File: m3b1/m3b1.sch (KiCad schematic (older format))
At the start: 16 parts, among them P5 MicroD-37Pins, Q1 MD3251, Q2 MD3251, U1 MC307, U2 MC306, U3 MC306, U4 MC306, U5 MC302, U6 MC306, U7 MC306, U8 MC301, U9 MC301

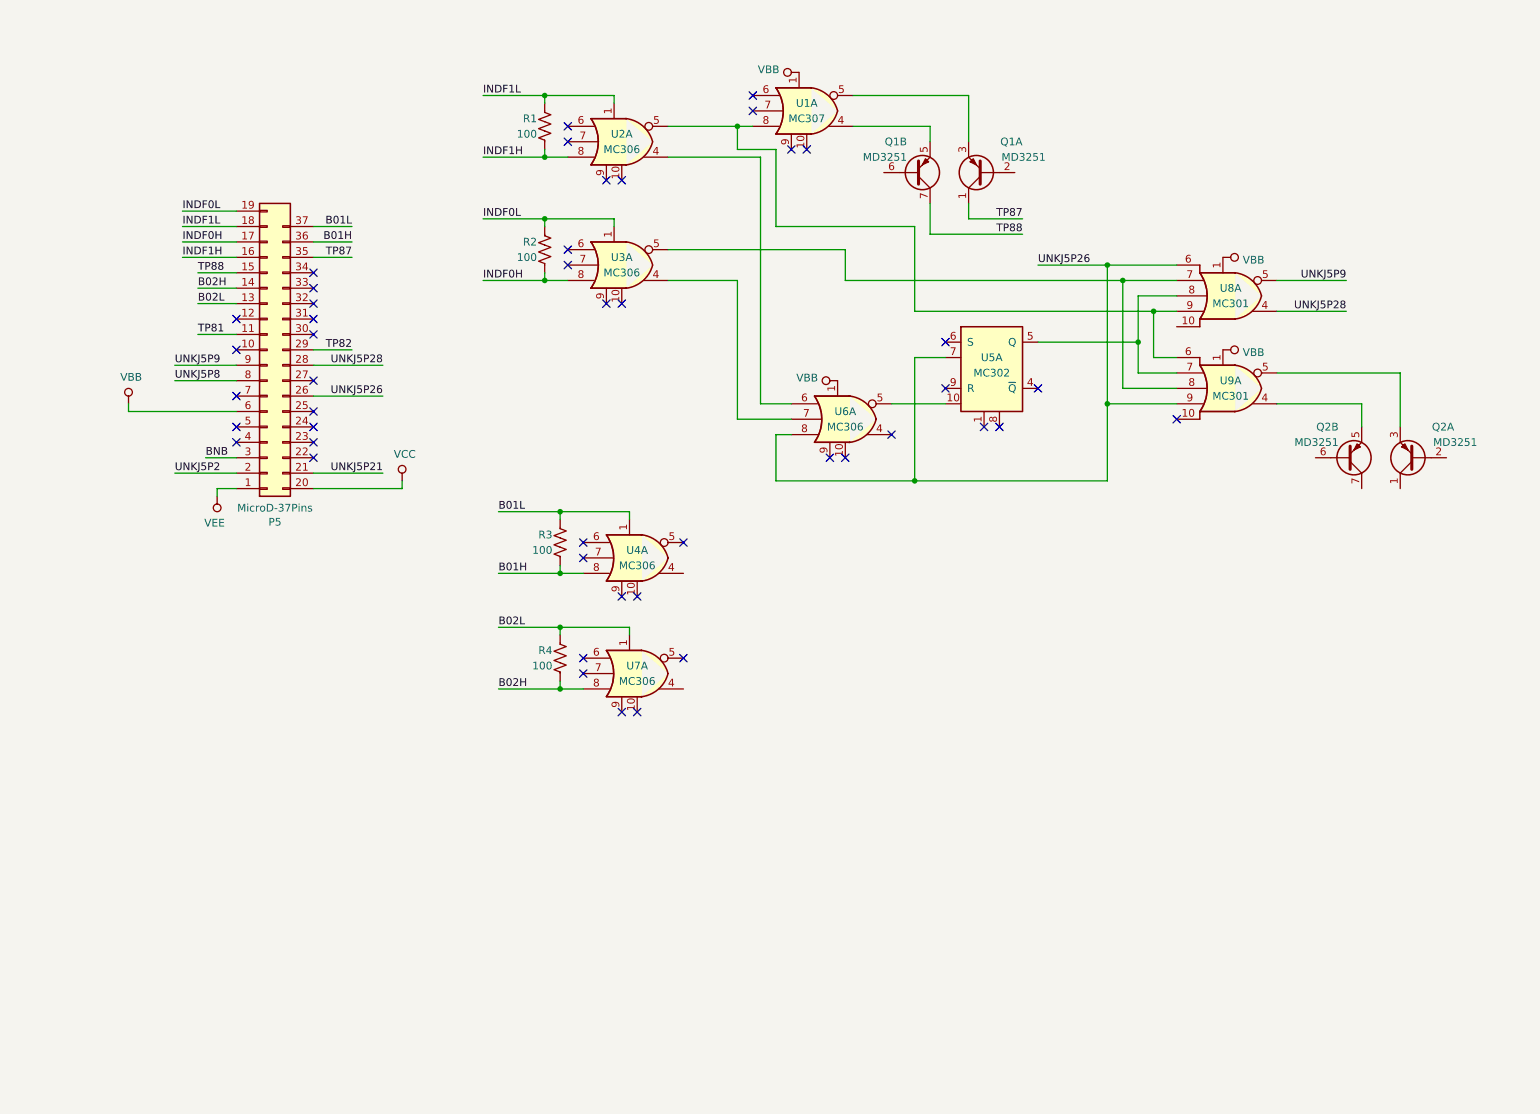
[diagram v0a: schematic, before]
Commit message: Completed initial schematic for module 3 board 1.
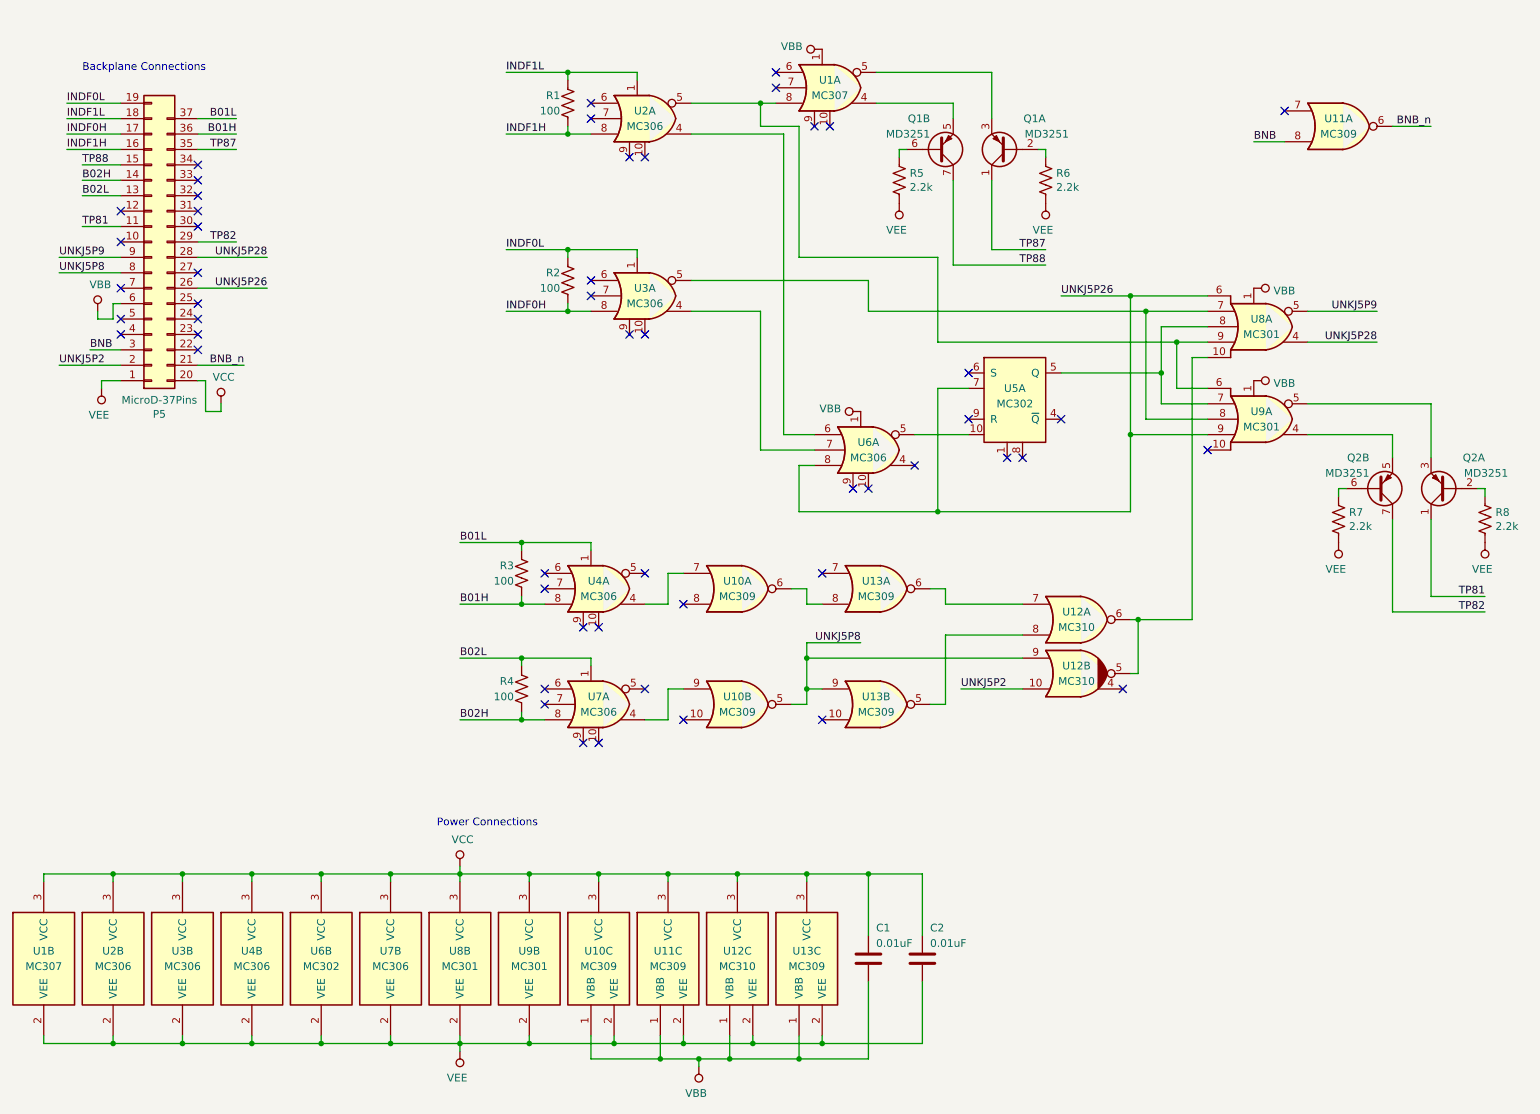
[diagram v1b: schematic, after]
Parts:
- added C1, C2: 0.01uF, symbol Device:C
- added R5, R6, R7, R8: 2.2k, symbol Device:R_US
- added unit 2 of U1
- added U10, U11, U13: MC309, symbol gn_buffer:MC309
- added U12: MC310, symbol gn_buffer:MC310
- added unit 2 of U2
- added unit 2 of U3
- added unit 2 of U4
- added unit 2 of U6
- added unit 2 of U7
- added unit 2 of U8
- added unit 2 of U9
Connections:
- net BNB: now also U11.8
- net TP81: now also Q2.1 (C1)
- net TP82: now also Q2.7 (C2)
- net UNKJ5P2: now also U12.10
- net UNKJ5P8: now also U10.5, U12.9, U13.9
- net VBB: now also C1.2, U10.1 (VBB), U11.1 (VBB), U12.1 (VBB), U13.1 (VBB)
- net VCC: now also C1.1, C2.1, U1.3 (VCC), U10.3 (VCC), U11.3 (VCC), U12.3 (VCC), U13.3 (VCC), U2.3 (VCC), U3.3 (VCC), U4.3 (VCC), U6.3 (VCC), U7.3 (VCC), U8.3 (VCC), U9.3 (VCC)
- net VEE: now also C2.2, R5.2, R6.2, R7.2, R8.2, U1.2 (VEE), U10.2 (VEE), U11.2 (VEE), U12.2 (VEE), U13.2 (VEE), U2.2 (VEE), U3.2 (VEE), U4.2 (VEE), U6.2 (VEE), U7.2 (VEE), U8.2 (VEE), U9.2 (VEE)
- net at U4.4: now also U10.7
- net at Q1.2 (B1): now also R6.1
- net at Q1.6 (B2): now also R5.1
- net at U7.4: now also U10.9
- net at U8.10: now also U12.5, U12.6
- net at Q2.2 (B1): now also R8.1
- net at Q2.6 (B2): now also R7.1
- net UNKJ5P21 renamed BNB_n
- net BNB_n: now also U11.6
- new net: U10.6, U13.8
- new net: U12.7, U13.6
- new net: U12.8, U13.5
- no-connect marks 46 -> 52
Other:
- note added: "Backplane Connections"
- note added: "Power Connections"
- moved on the sheet: P5, Q1A, Q1B, Q2A, Q2B, R1, R2, R3, R4, U1A, U2A, U3A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

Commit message: Eradicated net names taken from ME901-0666 -- the pinout was completely changed from early revs of that document.
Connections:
- net B01H renamed IN01H
- net B01L renamed IN01L
- net B02H renamed IN02H
- net B02L renamed IN02L
- net BNB renamed MC41
- net BNB_n renamed MC41_n
- net INDF0H renamed MC79
- net INDF0L renamed MC80
- net INDF1H renamed MC77
- net INDF1L renamed MC78
- net TP81 renamed MC81
- net TP82 renamed MC82
- net TP87 renamed MC87
- net TP88 renamed MC88
- net UNKJ5P26 renamed MC01
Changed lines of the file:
@@
 $EndDescr
 Text Label 2050 1500 2    50   ~ 0
-TP87
+MC87
 Wire Wire Line
 	1800 1500 2050 1500
 Text Label 2050 2100 2    50   ~ 0
-TP82
+MC82
 Wire Wire Line
 	1800 2100 2050 2100
 Text Label 1050 2000 0    50   ~ 0
-TP81
+MC81
 Wire Wire Line
 	1300 2000 1050 2000
-Text Label 950  1200 0    50   ~ 0
-INDF0L
-Wire Wire Line
-	1300 1200 950  1200
-Text Label 950  1400 0    50   ~ 0
-INDF0H
-Wire Wire Line
-	1300 1400 950  1400
-Text Label 950  1300 0    50   ~ 0
-INDF1L
-Wire Wire Line
-	1300 1300 950  1300
-Text Label 950  1500 0    50   ~ 0
-INDF1H
-Wire Wire Line
-	1300 1500 950  1500
+Text Label 1050 1200 0    50   ~ 0
+MC80
+Wire Wire Line
+	1300 1200 1050 1200
+Text Label 1050 1400 0    50   ~ 0
+MC79
+Wire Wire Line
+	1300 1400 1050 1400
+Text Label 1050 1300 0    50   ~ 0
+MC78
+Wire Wire Line
+	1300 1300 1050 1300
+Text Label 1050 1500 0    50   ~ 0
+MC77
+Wire Wire Line
+	1300 1500 1050 1500
 Text Label 1100 2800 0    50   ~ 0
-BNB
+MC41
 Wire Wire Line
 	1300 2800 1100 2800
 Text Label 1050 1800 0    50   ~ 0
-B02L
+IN02L
 Wire Wire Line
 	1300 1800 1050 1800
 Text Label 1050 1700 0    50   ~ 0
-B02H
+IN02H
 Wire Wire Line
 	1300 1700 1050 1700
 Text Label 2050 1300 2    50   ~ 0
-B01L
+IN01L
 Wire Wire Line
 	1800 1300 2050 1300
 Text Label 2050 1400 2    50   ~ 0
-B01H
+IN01H
 Wire Wire Line
 	1800 1400 2050 1400
@@
 	1300 1600 1050 1600
 Text Label 1050 1600 0    50   ~ 0
-TP88
+MC88
 NoConn ~ 1800 1700
 Wire Wire Line
@@
 Connection ~ 3900 4450
 Text Label 3500 4450 0    50   ~ 0
-B01H
+IN01H
 Wire Wire Line
 	3900 4050 3500 4050
 Connection ~ 3900 4050
 Text Label 3500 4050 0    50   ~ 0
-B01L
+IN01L
 NoConn ~ 4700 4250
 $Comp
@@
 Connection ~ 4200 2550
 Text Label 3800 2550 0    50   ~ 0
-INDF0H
+MC79
 Wire Wire Line
 	4200 2150 3800 2150
 Connection ~ 4200 2150
 Text Label 3800 2150 0    50   ~ 0
-INDF0L
+MC80
 $Comp
 L gn_buffer:MC306 U2
@@
 Connection ~ 4200 1400
 Text Label 3800 1400 0    50   ~ 0
-INDF1H
+MC77
 Wire Wire Line
 	4200 1000 3800 1000
 Connection ~ 4200 1000
 Text Label 3800 1000 0    50   ~ 0
-INDF1L
+MC78
 $Comp
 L gn_buffer:MC307 U1
@@
 	6950 2150 7300 2150
 Text Label 7300 2150 2    50   ~ 0
-TP87
+MC87
 Text Label 7300 2250 2    50   ~ 0
-TP88
+MC88
 $Comp
 L gn_buffer:MC306 U7
@@
 Connection ~ 3900 5200
 Text Label 3500 5200 0    50   ~ 0
-B02H
+IN02H
 Wire Wire Line
 	3900 4800 3500 4800
 Connection ~ 3900 4800
 Text Label 3500 4800 0    50   ~ 0
-B02L
+IN02L
 NoConn ~ 4700 5000
 $Comp
@@
 UNKJ5P28
 Wire Wire Line
-	1800 2400 2250 2400
-Text Label 2250 2400 2    50   ~ 0
-UNKJ5P26
+	1800 2400 2050 2400
+Text Label 2050 2400 2    50   ~ 0
+MC01
 Wire Wire Line
 	1800 2900 2100 2900
 Text Label 2100 2900 2    50   ~ 0
-BNB_n
+MC41_n
 Text Label 900  2900 0    50   ~ 0
 UNKJ5P2
@@
 	8350 2450 7850 2450
 Text Label 7400 2450 0    50   ~ 0
-UNKJ5P26
+MC01
 Wire Wire Line
 	7850 2450 7850 3350
@@
 NoConn ~ 8850 1250
 Text Label 8650 1450 0    50   ~ 0
-BNB
+MC41
 Wire Wire Line
 	9550 1350 9800 1350
 Text Label 9800 1350 2    50   ~ 0
-BNB_n
+MC41_n
 $Comp
 L Device:R_US R7
@@
 $EndComp
 Text Label 10150 4500 2    50   ~ 0
-TP82
+MC82
 Wire Wire Line
 	9550 4500 10150 4500
@@
 	9550 3900 9550 4500
 Text Label 10150 4400 2    50   ~ 0
-TP81
+MC81
 Wire Wire Line
 	9800 4400 10150 4400
